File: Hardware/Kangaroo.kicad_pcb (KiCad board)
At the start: 2 copper layers, 14 parts, among them J1 Conn_01x06_Pin, J2 Conn_01x06_Pin, U1 LM2588S-ADJ

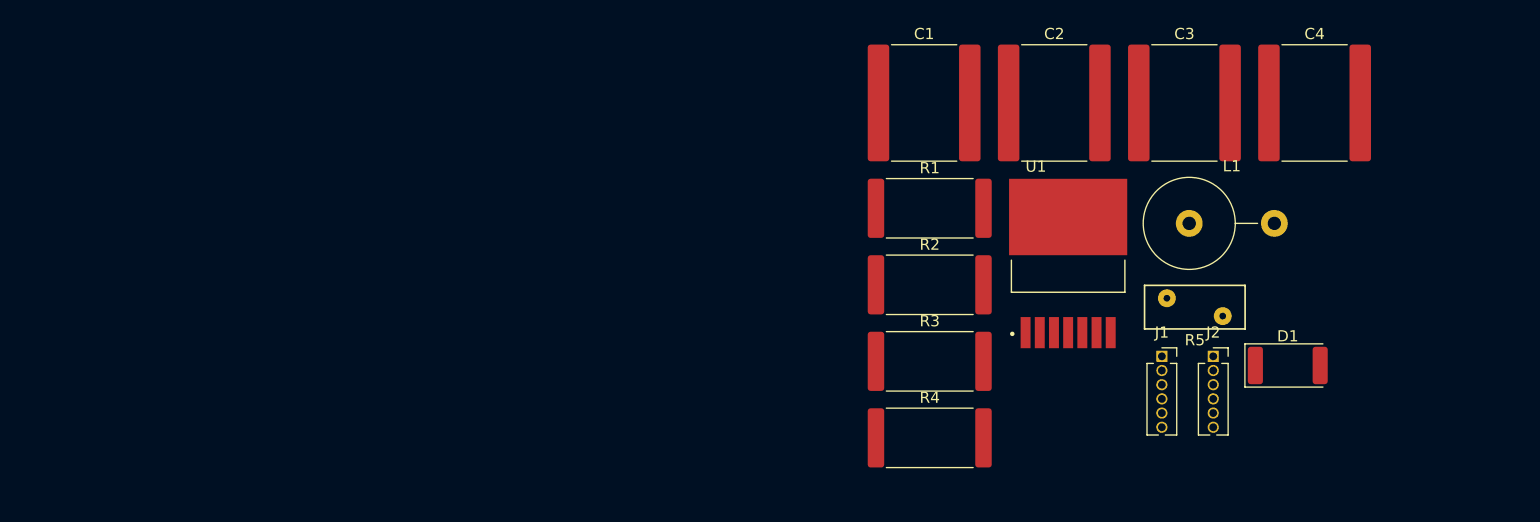
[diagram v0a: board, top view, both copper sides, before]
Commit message: Changed Schematic  & Footprints Symbols Added
New correct footprints added
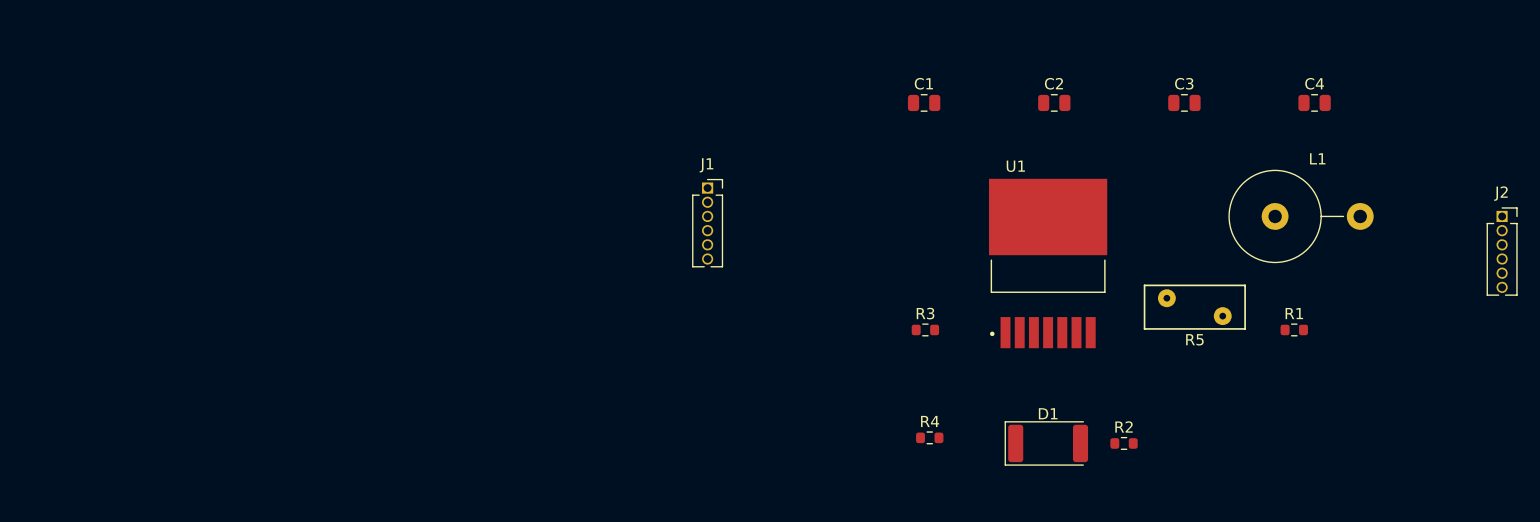
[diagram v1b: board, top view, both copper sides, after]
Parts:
- C1, C2, C3, C4: footprint Capacitor_SMD:C_3640_9110Metric -> Capacitor_SMD:C_0805_2012Metric
- R1, R2, R3, R4: footprint Resistor_SMD:R_4020_10251Metric -> Resistor_SMD:R_0603_1608Metric
- moved J1 43.4 mm to (127.0, 71.1)
- moved R1 34.4 mm to (179.5, 83.8)
- moved J2 28.7 mm to (198.1, 73.7)
- moved D1 22.6 mm to (157.5, 94.0)
- moved R2 22.5 mm to (164.3, 94.0)
- moved L1 7.71 mm to (177.8, 73.7)
- moved R3 2.84 mm to (146.5, 83.8)
- moved U1 1.79 mm to (157.5, 77.9)

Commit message: Changed Positions of Symbols
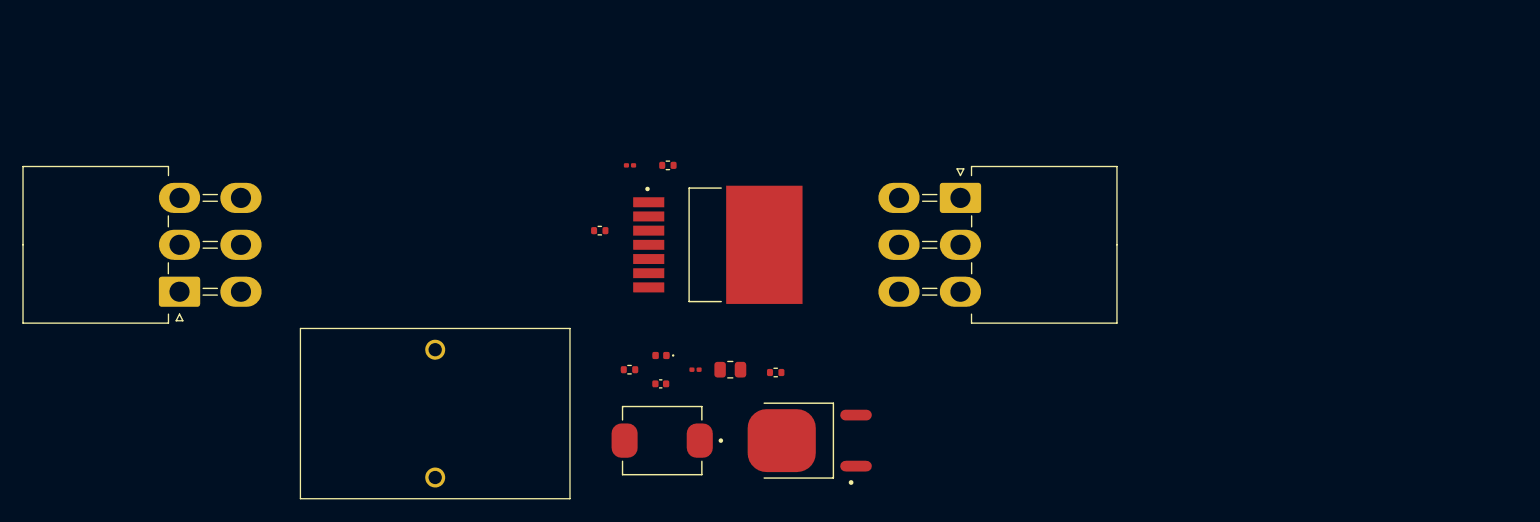
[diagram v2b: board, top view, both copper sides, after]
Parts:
- removed R3: R, Resistor_SMD:R_0603_1608Metric
- added CR2: SBR1045, iclr:DPAK228P990X239-4N, F.Cu at (136.1, 93.7)
- added D2: B540C-13-F, iclr:DIOM6959X245N, F.Cu at (122.9, 93.7)
- C1, C3: footprint Capacitor_SMD:C_0805_2012Metric -> Capacitor_SMD:C_0201_0603Metric
- C2: footprint Capacitor_SMD:C_0805_2012Metric -> Capacitor_SMD:C_0402_1005Metric
- C4: footprint Capacitor_SMD:C_0805_2012Metric -> Resistor_SMD:R_0805_2012Metric
- D1: footprint LED_SMD:LED_2512_6332Metric -> LED_SMD:LED_0402_1005Metric
- J1, J2: footprint Connector_PinSocket_1.27mm:PinSocket_1x06_P1.27mm_Vertical -> iclr:Molex_Mini-Fit_Jr_5569-06A2_2x03_P4.20mm_Horizontal_No_Mounting_Holes
- L1: value L -> P0848NL; footprint Inductor_THT:L_Axial_L20.0mm_D8.0mm_P7.62mm_Vertical -> iclr:P0848NL
- R1: value 3K -> 24.5K; footprint Resistor_SMD:R_0603_1608Metric -> Resistor_SMD:R_0402_1005Metric
- R2: value 1K -> 350; footprint Resistor_SMD:R_0603_1608Metric -> Resistor_SMD:R_0402_1005Metric
- R4: value R -> 3K; footprint Resistor_SMD:R_0603_1608Metric -> Resistor_SMD:R_0402_1005Metric
- R5: value R_Variable -> 1K; footprint Varistor:RV_Disc_D9mm_W3.9mm_P5mm -> Resistor_SMD:R_0402_1005Metric
- moved J2 118.6 mm to (79.7, 80.4), turned to 90 degrees
- moved L1 78.7 mm to (102.6, 97.0), turned to 90 degrees
- moved R1 62.8 mm to (117.3, 74.9)
- moved C4 57.5 mm to (129.0, 87.4)
- moved C3 49.9 mm to (120.1, 69.1)
- moved R5 48.5 mm to (120.0, 87.4)
- moved R2 47.8 mm to (123.4, 69.1)
- moved C2 43.3 mm to (122.8, 88.6)
- moved D1 35.5 mm to (122.8, 86.1), turned to 180 degrees
- moved C1 31.4 mm to (125.9, 87.4)
- moved U1 29.6 mm to (127.9, 76.2), turned to -90 degrees
- moved J1 22.7 mm to (149.6, 72.0), turned to -90 degrees
- moved R4 15.0 mm to (133.1, 87.6)
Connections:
- R1 pad 1: Net-(U1-COMP) -> Net-(J1-Pin_2)
- R1 pad 2: Net-(C4-Pad1) -> Net-(U1-FB)
- R2 pad 1: Net-(U1-VIN) -> Net-(U1-FB)
- R2 pad 2: Net-(D1-A) -> Net-(D1-K)
- R4 pad 1: Net-(U1-FB) -> Net-(U1-COMP)
- R4 pad 2: Net-(D1-K) -> Net-(C4-Pad1)
- R5 pad 1: Net-(R3-Pad2) -> Net-(U1-VIN)
- R5 pad 2: Net-(U1-FB) -> Net-(D1-A)
